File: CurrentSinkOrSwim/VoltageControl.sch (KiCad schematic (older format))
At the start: 7 parts

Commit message: Schematic annotate
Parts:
- gave numbers to parts that had none: 7
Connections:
- net at R201.1, RV201.3: now also U201.3 (+); no longer U201.5 (+)
- net at R202.2, R203.1: now also U201.2 (-); no longer U201.6 (-)
- net at D201.2 (K): now also U201.1; no longer U201.7
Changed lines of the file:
@@
 Sheet 2 4
 Title ""
-Date "1 sep 2015"
+Date "6 sep 2015"
 Rev ""
 Comp ""
@@
 $EndDescr
 $Comp
-L LMV358 U?
-U 2 1 55E5F043
+L LMV358 U201
+U 1 1 55E5F043
 P 5950 3700
-F 0 "U?" H 5900 3900 60  0000 L CNN
+F 0 "U201" H 5900 3900 60  0000 L CNN
 F 1 "LMV358" H 5900 3450 60  0000 L CNN
 F 2 "" H 5950 3700 60  0000 C CNN
 F 3 "" H 5950 3700 60  0000 C CNN
-	2    5950 3700
+	1    5950 3700
 	1    0    0    -1
 $EndComp
 $Comp
-L R R?
+L R R201
 U 1 1 55E5F049
 P 3600 5200
-F 0 "R?" V 3680 5200 40  0000 C CNN
+F 0 "R201" V 3680 5200 40  0000 C CNN
 F 1 "R" V 3607 5201 40  0000 C CNN
 F 2 "~" V 3530 5200 30  0000 C CNN
@@
 $EndComp
 $Comp
-L GND #PWR?
+L GND #PWR202
 U 1 1 55E5F04F
 P 5850 4250
-F 0 "#PWR?" H 5850 4250 30  0001 C CNN
+F 0 "#PWR202" H 5850 4250 30  0001 C CNN
 F 1 "GND" H 5850 4180 30  0001 C CNN
 F 2 "~" H 5850 4250 60  0000 C CNN
@@
 $EndComp
 $Comp
-L POT RV?
+L POT RV201
 U 1 1 55E5F055
 P 3600 4350
-F 0 "RV?" H 3600 4250 50  0000 C CNN
+F 0 "RV201" H 3600 4250 50  0000 C CNN
 F 1 "POT" H 3600 4350 50  0000 C CNN
 F 2 "~" H 3600 4350 60  0000 C CNN
@@
 $EndComp
 $Comp
-L C C?
+L C C201
 U 1 1 55E5F05B
 P 5350 3200
-F 0 "C?" H 5350 3300 40  0000 L CNN
+F 0 "C201" H 5350 3300 40  0000 L CNN
 F 1 "C" H 5356 3115 40  0000 L CNN
 F 2 "~" H 5388 3050 30  0000 C CNN
@@
 $EndComp
 $Comp
-L GND #PWR?
+L GND #PWR201
 U 1 1 55E5F061
 P 5350 3450
-F 0 "#PWR?" H 5350 3450 30  0001 C CNN
+F 0 "#PWR201" H 5350 3450 30  0001 C CNN
 F 1 "GND" H 5350 3380 30  0001 C CNN
 F 2 "~" H 5350 3450 60  0000 C CNN
@@
 	6450 3700 6800 3700
 $Comp
-L DIODE D?
+L DIODE D201
 U 1 1 55E5F084
 P 7000 3700
-F 0 "D?" H 7000 3800 40  0000 C CNN
+F 0 "D201" H 7000 3800 40  0000 C CNN
 F 1 "DIODE" H 7000 3600 40  0000 C CNN
 F 2 "~" H 7000 3700 60  0000 C CNN
@@
 $EndComp
 $Comp
-L R R?
+L R R202
 U 1 1 55E5F0BD
 P 8600 4100
-F 0 "R?" V 8680 4100 40  0000 C CNN
+F 0 "R202" V 8680 4100 40  0000 C CNN
 F 1 "9K" V 8607 4101 40  0000 C CNN
 F 2 "~" V 8530 4100 30  0000 C CNN
@@
 $EndComp
 $Comp
-L R R?
+L R R203
 U 1 1 55E5F0C3
 P 8600 5000
-F 0 "R?" V 8680 5000 40  0000 C CNN
+F 0 "R203" V 8680 5000 40  0000 C CNN
 F 1 "1K" V 8607 5001 40  0000 C CNN
 F 2 "~" V 8530 5000 30  0000 C CNN

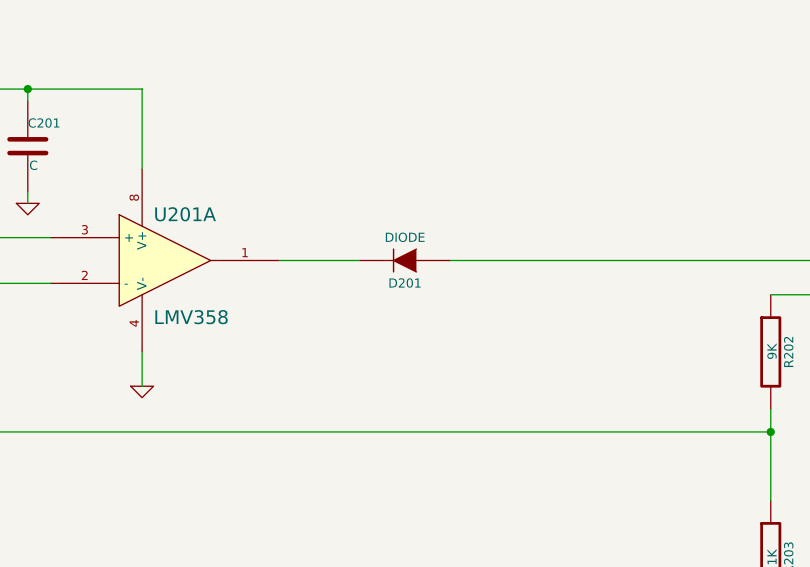
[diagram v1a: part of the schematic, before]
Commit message: Añadiendo net list, footprints y nombres a los componentes que no lo tenían. Empezando con el layout
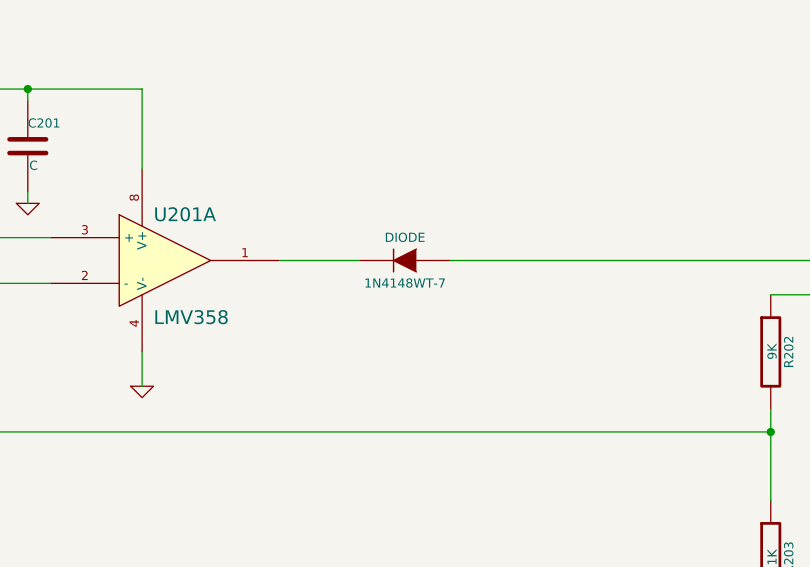
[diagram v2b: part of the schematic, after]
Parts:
- 1N4148WT-7: renamed from D201; MFG Part Number (none) -> 1N4148WT-7
- U201: Distributor Part Number 1 (none) -> http://www.farnell.com/datasheets/1862405.pdf; MFG Part Number (none) -> LMV358ID
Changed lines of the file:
@@
 F 2 "" H 5950 3700 60  0000 C CNN
 F 3 "" H 5950 3700 60  0000 C CNN
+F 4 " LMV358ID" H 5950 3700 60  0001 C CNN "MFG Part Number"
+F 5 "http://www.farnell.com/datasheets/1862405.pdf" H 5950 3700 60  0001 C CNN "Distributor Part Number 1"
 	1    5950 3700
 	1    0    0    -1
@@
 $EndComp
 $Comp
-L GND #PWR202
+L GND #PWR03
 U 1 1 55E5F04F
 P 5850 4250
-F 0 "#PWR202" H 5850 4250 30  0001 C CNN
+F 0 "#PWR03" H 5850 4250 30  0001 C CNN
 F 1 "GND" H 5850 4180 30  0001 C CNN
 F 2 "~" H 5850 4250 60  0000 C CNN
@@
 $EndComp
 $Comp
-L GND #PWR201
+L GND #PWR04
 U 1 1 55E5F061
 P 5350 3450
-F 0 "#PWR201" H 5350 3450 30  0001 C CNN
+F 0 "#PWR04" H 5350 3450 30  0001 C CNN
 F 1 "GND" H 5350 3380 30  0001 C CNN
 F 2 "~" H 5350 3450 60  0000 C CNN
@@
 	6450 3700 6800 3700
 $Comp
-L DIODE D201
+L DIODE 1N4148WT-7
 U 1 1 55E5F084
 P 7000 3700
-F 0 "D201" H 7000 3800 40  0000 C CNN
+F 0 "1N4148WT-7" H 7000 3800 40  0000 C CNN
 F 1 "DIODE" H 7000 3600 40  0000 C CNN
 F 2 "~" H 7000 3700 60  0000 C CNN
-F 3 "~" H 7000 3700 60  0000 C CNN
+F 3 "http://www.farnell.com/datasheets/1915502.pdf" H 7000 3700 60  0001 C CNN
+F 4 "1N4148WT-7" H 7000 3700 60  0001 C CNN "MFG Part Number"
 	1    7000 3700
 	-1   0    0    1
